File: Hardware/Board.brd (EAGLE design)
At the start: 40 x 72 mm, 51 parts, among them J1 OUT, J2 POWER, J3 ICSP, U1 ATTINY2313A, U2 AW9523B

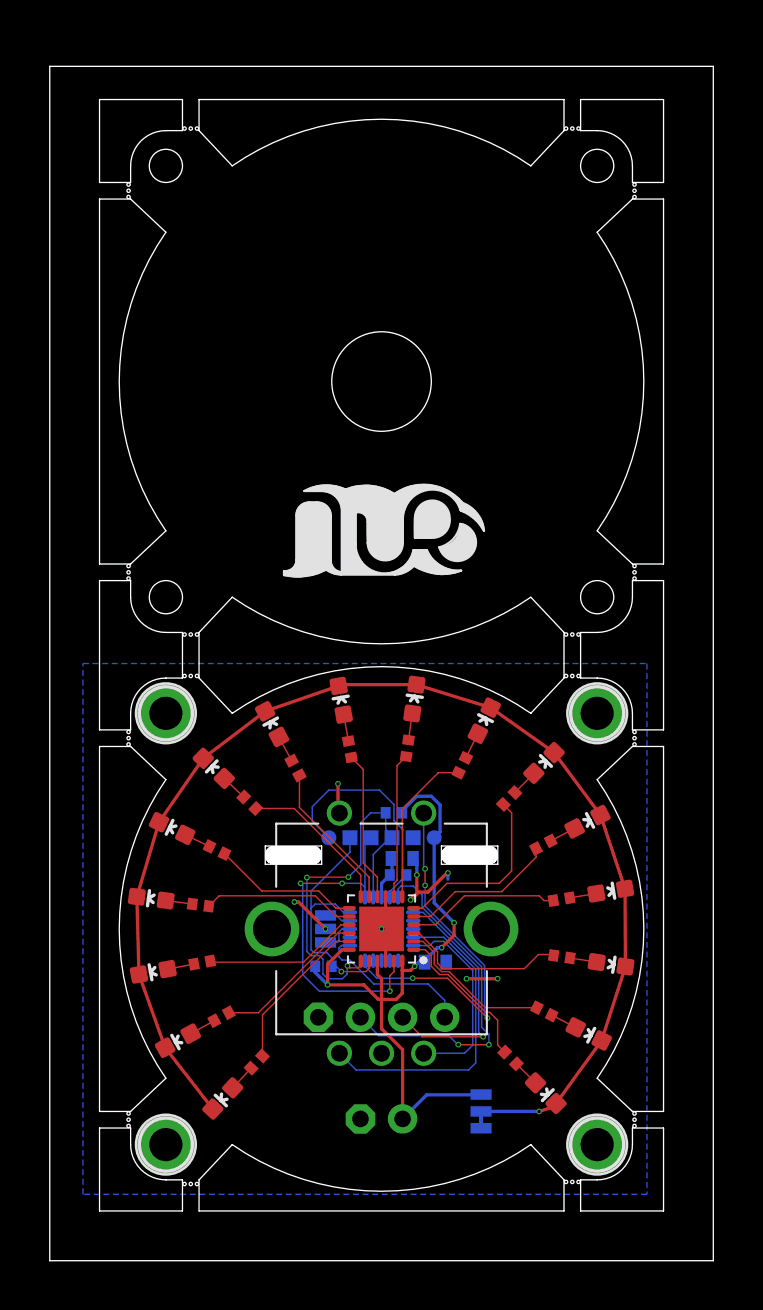
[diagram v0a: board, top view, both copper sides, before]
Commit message: updated board layout to optimize for DFM
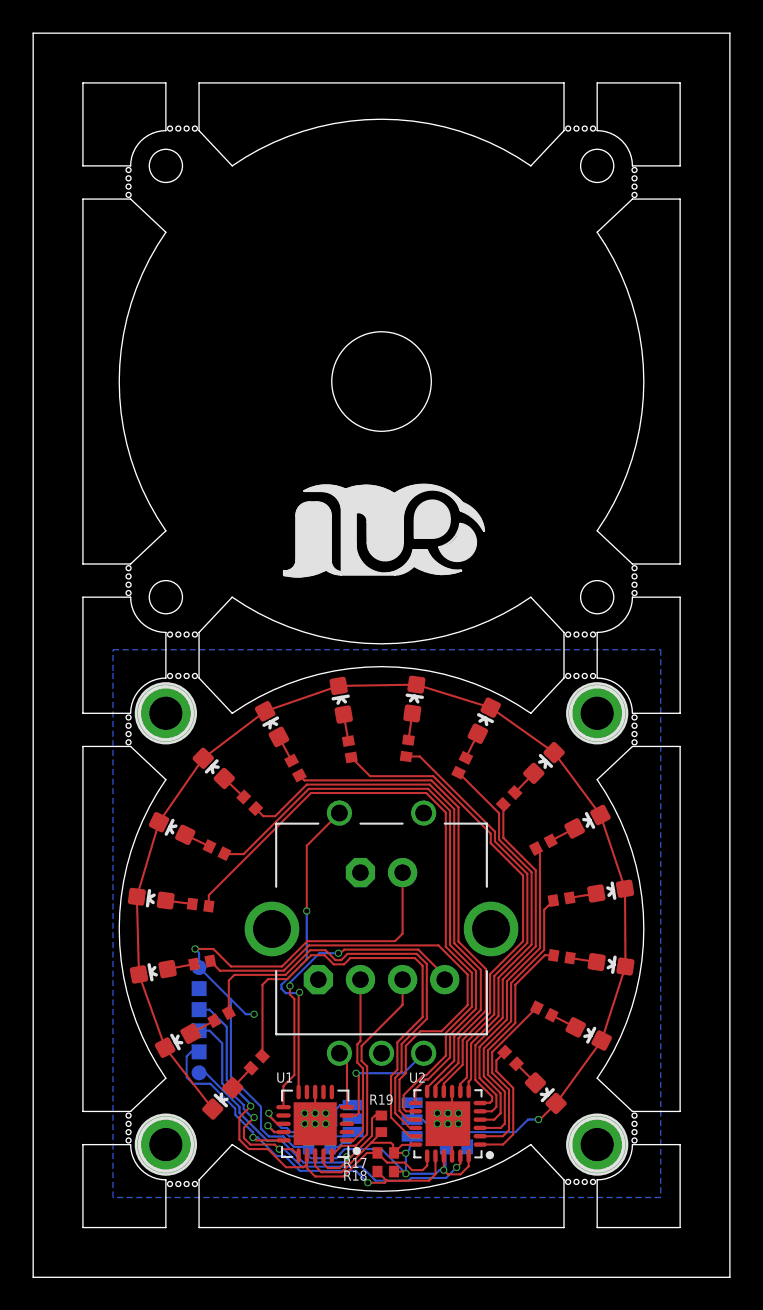
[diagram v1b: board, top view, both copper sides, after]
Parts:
- J3: device MiniISP:MINI-ISP-LOCK -> MiniISP:MINI-ISP-LABELS
- moved R17 20.5 mm to (20.3, 6.50), flipped to the top, turned to 0 degrees
- moved C1 18.1 mm to (16.3, 6.86)
- moved J3 15.6 mm to (9.00, 14.5), turned to 90 degrees
- moved R19 15.0 mm to (20.0, 8.26), flipped to the top, turned to 270 degrees
- moved J2 14.8 mm to (20.0, 22.8)
- moved R18 12.9 mm to (20.3, 5.38), flipped to the top
- moved U2 12.4 mm to (24.0, 8.26)
- moved U1 12.4 mm to (16.0, 8.26), flipped to the top, turned to 180 degrees
- moved JP2 11.6 mm to (18.3, 8.57), turned to 90 degrees
- moved C2 11.2 mm to (24.5, 6.86)
- moved JP1 4.19 mm to (21.8, 8.51), turned to 90 degrees
- moved J1 2.27 mm to (20.0, 16.4)
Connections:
- removed net VCC: C1.1, R19.2, U1.18
- new net N$45: JP1.2, LED1.C, LED10.C, LED11.C, LED12.C, LED13.C, LED14.C, LED15.C, LED16.C, LED2.C, LED3.C, LED4.C, LED5.C, LED6.C, LED7.C, LED8.C, LED9.C
- net +5V: now also C1.1, R19.2, U1.18
- net GND: now also SW1.SW+; no longer JP1.2, LED1.C, LED10.C, LED11.C, LED12.C, LED13.C, LED14.C, LED15.C, LED16.C, LED2.C, LED3.C, LED4.C, LED5.C, LED6.C, LED7.C, LED8.C, LED9.C, SW1.SW-
- net N$20: now also J1.3; no longer J1.2
- net N$37: now also SW1.A; no longer SW1.B
- net N$38: now also SW1.SW-; no longer SW1.SW+
- net N$39: now also J1.2; no longer J1.3
- net N$40: now also SW1.B; no longer SW1.A
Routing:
- net GND: track 93.0 -> 8.98 mm, vias 10 -> 12
- net N$45: track 0.00 -> 80.0 mm, vias 0 -> 1
- net N$33: track 9.24 -> 39.1 mm
- net N$28: track 8.89 -> 35.7 mm
- net N$27: track 9.30 -> 32.6 mm
- net N$26: track 9.05 -> 29.5 mm
- net +5V: track 42.3 -> 62.5 mm, vias 4 -> 5
- net N$34: track 9.33 -> 29.0 mm
- net N$25: track 9.05 -> 28.6 mm
- net N$36: track 9.55 -> 27.2 mm
- net N$35: track 9.25 -> 26.7 mm
- net N$24: track 8.75 -> 25.4 mm
- net N$23: track 9.60 -> 22.6 mm
- net N$40: track 19.0 -> 7.82 mm, vias 0 -> 1
- net N$22: track 11.0 -> 21.4 mm
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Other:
- board size 40 x 72 mm -> 42 x 75 mm
- board text added: "!SR / PT"
- board text added: "+5V"
- board text added: "1"
- board text added: "2"
- board text added: "2 TX A"
- board text added: "3 RX B"
- board text added: "4 DR SW"
- board text added: "GND"
- board text added: "J2"
- board text added: "JP2: Output Mode: !SD = Serial (9600 Baud) PT = Passthrough (Graycode)"
- board text added: "Mini ICSP"
- board text removed: "!SD / PT"
- board text removed: "Mini- ICSP"
- board text removed: "Output Mode: !SD = Step / Direction PT = Passthrough (Graycode)"

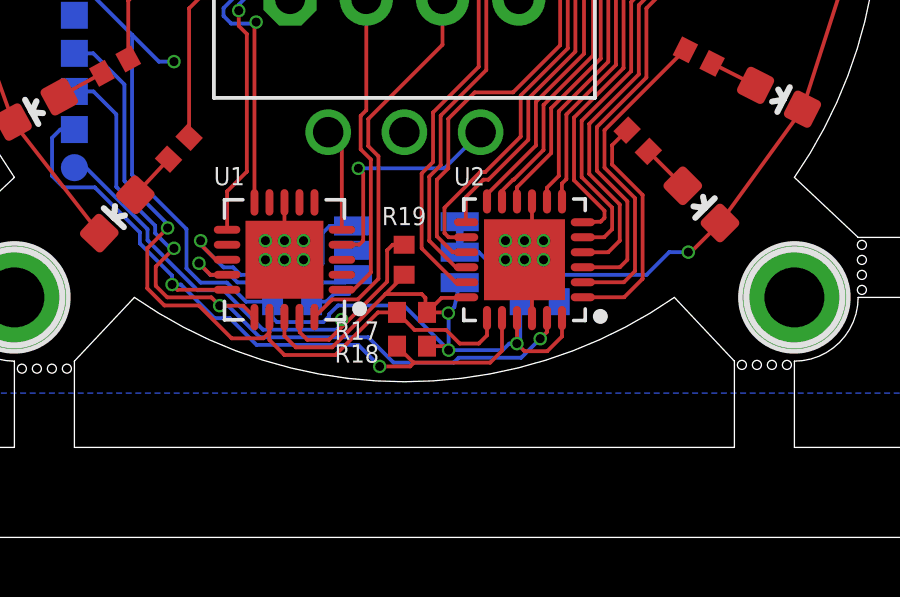
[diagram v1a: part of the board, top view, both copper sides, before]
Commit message: updated hardware files with latest production run
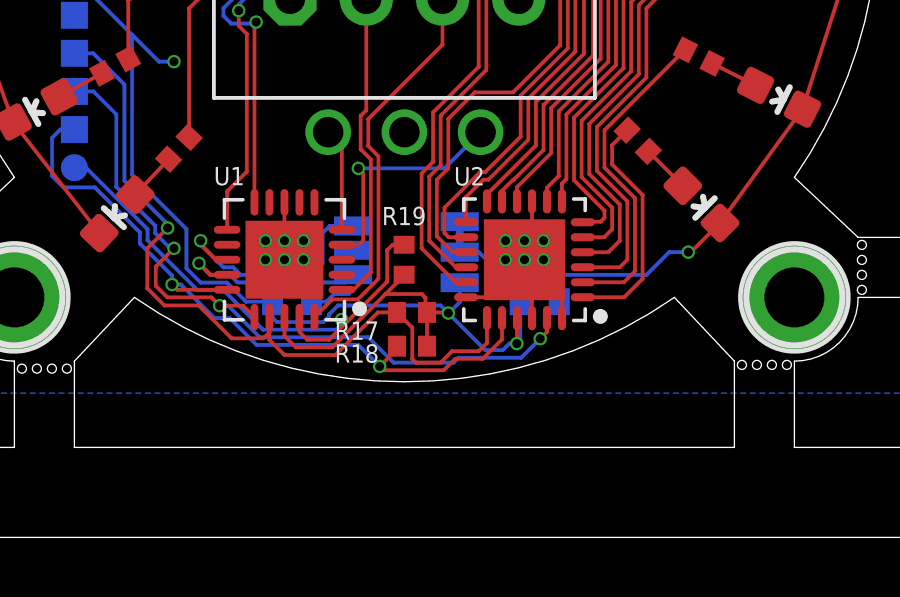
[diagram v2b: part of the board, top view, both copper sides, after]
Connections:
- net +5V: no longer U2.18, U2.24
- net GND: now also U2.18, U2.24
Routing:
- net +5V: track 62.5 -> 57.7 mm, vias 5 -> 4
- net GND: track 8.98 -> 13.5 mm
- net N$18: track 24.5 -> 25.8 mm
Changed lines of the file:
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@@
 <drawing>
 <settings>
-<setting alwaysvectorfont="yes"/>
+<setting alwaysvectorfont="no"/>
 <setting verticaltext="up"/>
 </settings>
-<grid distance="50" unitdist="mil" unit="mil" style="lines" multiple="1" display="no" altdistance="5" altunitdist="mil" altunit="mil"/>
+<grid distance="1" unitdist="mm" unit="mm" style="lines" multiple="1" display="yes" altdistance="0.5" altunitdist="mm" altunit="mm"/>
 <layers>
 <layer number="1" name="Top" color="4" fill="1" visible="yes" active="yes"/>
@@
 <via x="16.637" y="8.89" extent="1-16" drill="0.3" shape="octagon"/>
 <via x="16.002" y="8.89" extent="1-16" drill="0.3" shape="octagon"/>
+<contactref element="U2" pad="18"/>
+<contactref element="U2" pad="24"/>
+<wire x1="25.253" y1="6.3099" x2="25.253" y2="7.005" width="0.127" layer="1"/>
+<wire x1="25.253" y1="7.005" x2="24.257" y2="8.001" width="0.127" layer="1"/>
+<wire x1="22.0579" y1="7.005" x2="22.753" y2="7.005" width="0.127" layer="1"/>
+<wire x1="22.753" y1="7.005" x2="24.003" y2="8.255" width="0.127" layer="1"/>
 </signal>
 <signal name="+5V">
@@
 <wire x1="17.5937875" y1="5.334" x2="19.3717875" y2="7.112" width="0.127" layer="1"/>
 <wire x1="20.701" y1="6.985" x2="20.574" y2="7.112" width="0.127" layer="1"/>
-<wire x1="21.239" y1="6.985" x2="22.0379" y2="6.985" width="0.127" layer="1"/>
-<wire x1="22.0379" y1="6.985" x2="22.0579" y2="7.005" width="0.127" layer="1"/>
 <wire x1="19.3717875" y1="7.112" x2="20.574" y2="7.112" width="0.127" layer="1"/>
-<wire x1="21.239" y1="6.985" x2="20.754" y2="6.5" width="0.127" layer="1"/>
 <wire x1="20.754" y1="6.5" x2="20.701" y2="6.553" width="0.127" layer="1"/>
 <wire x1="20.701" y1="6.553" x2="20.701" y2="6.985" width="0.127" layer="1"/>
-<wire x1="23.749" y1="5.461" x2="24.003" y2="5.207" width="0.127" layer="1"/>
-<wire x1="24.761325" y1="5.207" x2="24.003" y2="5.207" width="0.127" layer="1"/>
 <wire x1="23.749" y1="5.461" x2="23.753" y2="5.465" width="0.127" layer="1"/>
 <wire x1="23.753" y1="5.465" x2="23.753" y2="6.3099" width="0.127" layer="1"/>
@@
 <wire x1="23.749" y1="5.461" x2="23.495" y2="5.461" width="0.127" layer="16"/>
 <wire x1="23.495" y1="5.461" x2="23.2767" y2="5.2427" width="0.127" layer="16"/>
-<wire x1="23.2767" y1="5.2427" x2="21.47299375" y2="5.2427" width="0.127" layer="16"/>
-<via x="21.47299375" y="5.2427" extent="1-16" drill="0.3" shape="octagon"/>
-<wire x1="20.754" y1="5.375" x2="21.34069375" y2="5.375" width="0.127" layer="1"/>
-<wire x1="21.34069375" y1="5.375" x2="21.47299375" y2="5.2427" width="0.127" layer="1"/>
+<wire x1="23.2767" y1="5.2427" x2="22.6973" y2="5.2427" width="0.127" layer="16"/>
 <wire x1="20.754" y1="6.5" x2="21.44" y2="6.5" width="0.127" layer="1"/>
 <wire x1="21.44" y1="6.5" x2="21.463" y2="6.477" width="0.127" layer="1"/>
 <via x="21.463" y="6.477" extent="1-16" drill="0.3" shape="octagon"/>
 <wire x1="21.463" y1="6.477" x2="21.47299375" y2="6.46700625" width="0.127" layer="16"/>
-<wire x1="21.47299375" y1="6.46700625" x2="21.47299375" y2="5.2427" width="0.127" layer="16"/>
 <wire x1="23.749" y1="5.461" x2="23.861" y2="5.573" width="0.127" layer="16"/>
 <wire x1="23.861" y1="5.573" x2="23.861" y2="6.858" width="0.127" layer="16"/>
-<wire x1="19.98469375" y1="6.731" x2="21.47299375" y2="5.2427" width="0.127" layer="16"/>
 <wire x1="15.606" y1="6.858" x2="14.717" y2="6.858" width="0.127" layer="16"/>
 <wire x1="14.717" y1="6.858" x2="14.082" y2="7.493" width="0.127" layer="16"/>
@@
 <wire x1="12.319" y1="14.859" x2="11.816" y2="14.859" width="0.127" layer="16"/>
 <wire x1="11.816" y1="14.859" x2="10.922" y2="15.753" width="0.127" layer="16"/>
-<wire x1="21.463" y1="6.477" x2="21.666" y2="6.68" width="0.127" layer="16"/>
-<wire x1="21.844" y1="7.491" x2="21.666" y2="6.68" width="0.127" layer="16"/>
 <via x="8.763" y="18.796" extent="1-16" drill="0.3" shape="octagon"/>
 <wire x1="10.920509375" y1="17.738375" x2="9.867134375" y2="18.79175" width="0.127" layer="1"/>
@@
 <wire x1="9" y1="18.559" x2="9" y2="17.675" width="0.127" layer="16"/>
 <wire x1="10.920509375" y1="17.738375" x2="14.00178125" y2="17.738375" width="0.127" layer="1"/>
-<wire x1="24.761325" y1="5.207" x2="25.253" y2="5.698675" width="0.127" layer="1"/>
-<wire x1="25.253" y1="5.698675" x2="25.253" y2="6.3099" width="0.127" layer="1"/>
 <wire x1="21.27" y1="19.714" x2="21.27" y2="23.397" width="0.127" layer="1"/>
 <wire x1="21.27" y1="19.714" x2="20.818375" y2="19.262375" width="0.127" layer="1"/>
 <wire x1="14.00178125" y1="17.738375" x2="15.52578125" y2="19.262375" width="0.127" layer="1"/>
 <wire x1="15.52578125" y1="19.262375" x2="20.818375" y2="19.262375" width="0.127" layer="1"/>
-<contactref element="U2" pad="18"/>
 <contactref element="U2" pad="21"/>
-<contactref element="U2" pad="24"/>
 <wire x1="19.9898" y1="7.755" x2="19.9898" y2="7.7300125" width="0.127" layer="1"/>
 <wire x1="19.9898" y1="7.7300125" x2="19.3717875" y2="7.112" width="0.127" layer="1"/>
-<wire x1="17.78689375" y1="6.731" x2="19.98469375" y2="6.731" width="0.127" layer="16"/>
+<wire x1="17.78689375" y1="6.731" x2="21.209" y2="6.731" width="0.127" layer="16"/>
 <wire x1="15.606" y1="6.858" x2="15.606" y2="6.3207" width="0.127" layer="16"/>
 <wire x1="15.606" y1="6.3207" x2="15.748" y2="6.1787" width="0.127" layer="16"/>
@@
 <wire x1="17.4903" y1="6.37289375" x2="17.4903" y2="6.43440625" width="0.127" layer="16"/>
 <wire x1="15.748" y1="6.1787" x2="17.29610625" y2="6.1787" width="0.127" layer="16"/>
+<wire x1="21.844" y1="7.491" x2="21.844" y2="6.8380125" width="0.127" layer="16"/>
+<wire x1="21.844" y1="6.8380125" x2="21.47299375" y2="6.46700625" width="0.127" layer="16"/>
+<wire x1="20.754" y1="5.375" x2="20.754" y2="6.5" width="0.127" layer="1"/>
+<wire x1="21.463" y1="6.477" x2="21.209" y2="6.731" width="0.127" layer="16"/>
+<wire x1="21.463" y1="6.477" x2="22.6973" y2="5.2427" width="0.127" layer="16"/>
 </signal>
 <signal name="N$18">
@@
 <wire x1="10.668" y1="14.097" x2="9.63" y2="15.135" width="0.127" layer="16"/>
 <wire x1="14.2411625" y1="5.635603125" x2="13.145765625" y2="6.731" width="0.127" layer="1"/>
-<wire x1="19.754" y1="6.5" x2="20.3385" y2="5.9155" width="0.127" layer="1"/>
-<wire x1="21.3895" y1="5.9155" x2="21.844" y2="5.461" width="0.127" layer="1"/>
-<wire x1="21.844" y1="5.461" x2="22.479" y2="5.461" width="0.127" layer="1"/>
-<wire x1="22.479" y1="5.461" x2="22.753" y2="5.735" width="0.127" layer="1"/>
-<wire x1="22.753" y1="5.735" x2="22.753" y2="6.3099" width="0.127" layer="1"/>
-<wire x1="20.3385" y1="5.9155" x2="21.3895" y2="5.9155" width="0.127" layer="1"/>
 <contactref element="U2" pad="19"/>
 <wire x1="13.145765625" y1="6.731" x2="12.0000875" y2="6.731" width="0.127" layer="1"/>
@@
 <wire x1="11.43" y1="8.636" x2="12.108153125" y2="9.314153125" width="0.127" layer="1"/>
 <wire x1="11.43" y1="7.3010875" x2="11.43" y2="8.636" width="0.127" layer="1"/>
+<wire x1="19.754" y1="6.5" x2="20.2635" y2="5.9905" width="0.127" layer="1"/>
+<wire x1="20.2635" y1="4.94609375" x2="20.38359375" y2="4.826" width="0.127" layer="1"/>
+<wire x1="20.2635" y1="5.9905" x2="20.2635" y2="4.94609375" width="0.127" layer="1"/>
+<wire x1="20.38359375" y1="4.826" x2="21.209" y2="4.826" width="0.127" layer="1"/>
+<wire x1="21.209" y1="4.826" x2="21.59" y2="5.207" width="0.127" layer="1"/>
+<wire x1="21.59" y1="5.207" x2="22.479" y2="5.207" width="0.127" layer="1"/>
+<wire x1="22.479" y1="5.207" x2="22.753" y2="5.481" width="0.127" layer="1"/>
+<wire x1="22.753" y1="5.481" x2="22.753" y2="6.3099" width="0.127" layer="1"/>
 </signal>
 <signal name="N$40">
@@
 <contactref element="J3" pad="MOSI"/>
 <via x="19.177" y="4.699" extent="1-16" drill="0.3" shape="octagon"/>
-<wire x1="19.754" y1="5.375" x2="20.303" y2="4.826" width="0.127" layer="1"/>
-<wire x1="20.32" y1="4.826" x2="20.193" y2="4.699" width="0.127" layer="1"/>
-<wire x1="20.193" y1="4.699" x2="19.177" y2="4.699" width="0.127" layer="1"/>
-<wire x1="23.253" y1="5.219" x2="23.253" y2="6.3099" width="0.127" layer="1"/>
-<wire x1="20.32" y1="4.826" x2="20.303" y2="4.826" width="0.127" layer="1"/>
-<wire x1="20.32" y1="4.826" x2="22.86" y2="4.826" width="0.127" layer="1"/>
-<wire x1="22.86" y1="4.826" x2="23.253" y2="5.219" width="0.127" layer="1"/>
+<wire x1="23.253" y1="5.6" x2="23.253" y2="6.3099" width="0.127" layer="1"/>
+<wire x1="22.606" y1="4.953" x2="23.253" y2="5.6" width="0.127" layer="1"/>
 <wire x1="12.547459375" y1="7.429934375" x2="12.25575" y2="7.429934375" width="0.127" layer="16"/>
 <contactref element="U2" pad="20"/>
@@
 <wire x1="12.25575" y1="7.726825" x2="12.25575" y2="7.429934375" width="0.127" layer="16"/>
 <wire x1="11.18345625" y1="8.79911875" x2="12.25575" y2="7.726825" width="0.127" layer="16"/>
+<wire x1="19.304" y1="4.572" x2="19.177" y2="4.699" width="0.127" layer="1"/>
+<wire x1="19.754" y1="5.375" x2="19.754" y2="5.276" width="0.127" layer="1"/>
+<wire x1="19.754" y1="5.276" x2="19.177" y2="4.699" width="0.127" layer="1"/>
+<wire x1="21.6952125" y1="4.953" x2="22.606" y2="4.953" width="0.127" layer="1"/>
+<wire x1="21.6952125" y1="4.953" x2="21.3142125" y2="4.572" width="0.127" layer="1"/>
+<wire x1="21.3142125" y1="4.572" x2="19.304" y2="4.572" width="0.127" layer="1"/>
 </signal>
 <signal name="N$19">
